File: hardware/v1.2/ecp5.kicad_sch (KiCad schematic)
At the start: 8 parts, among them U1 ECP5U_25F_CABGA256

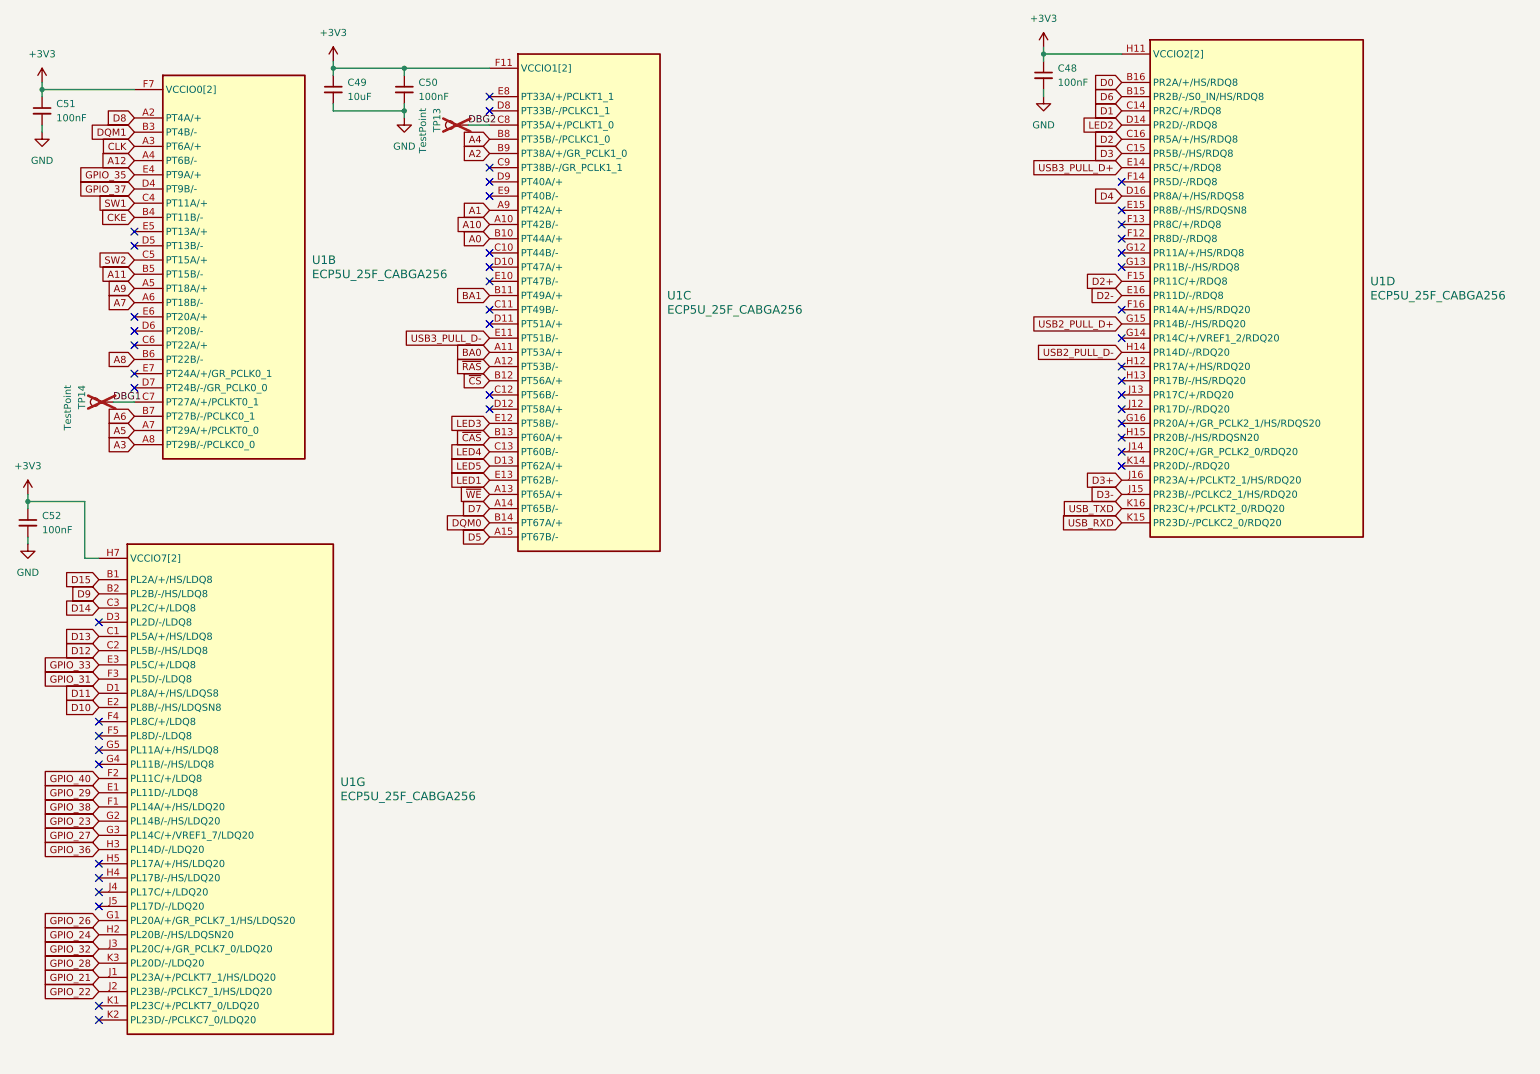
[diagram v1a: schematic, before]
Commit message: Custom ECP5-CABGA256 symbol
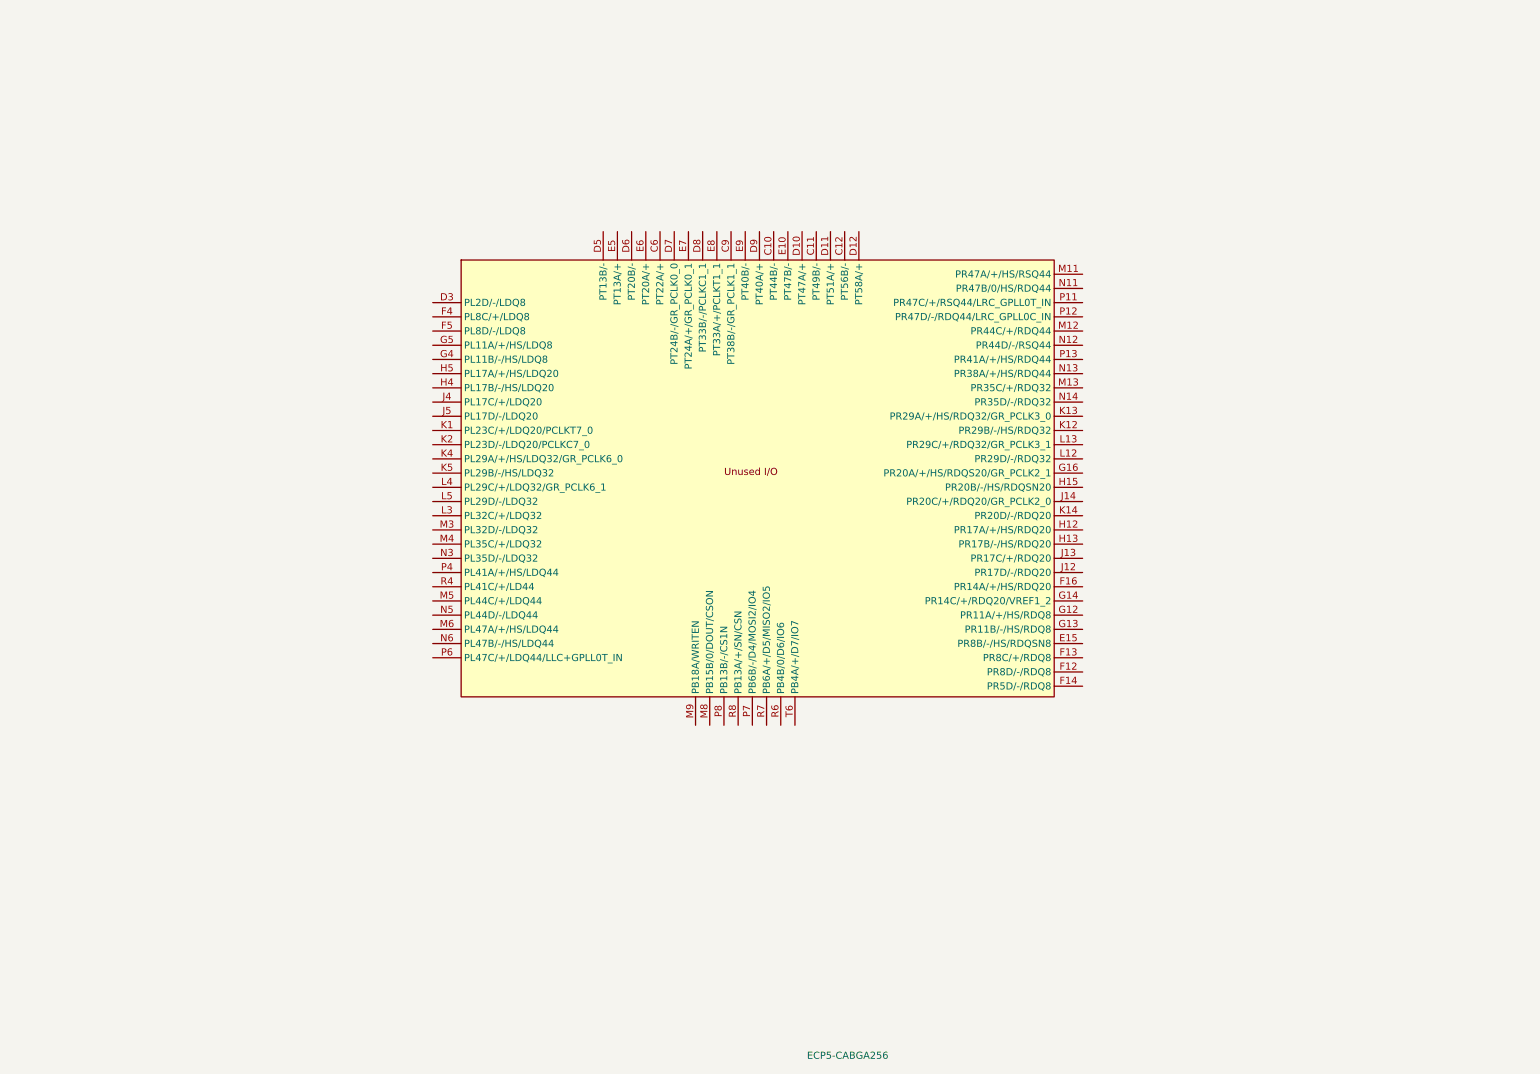
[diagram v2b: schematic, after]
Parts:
- removed C48, C50, C51, C52: 100nF, Capacitor_SMD:C_0402_1005Metric, symbol Device:C_Small
- removed C49: 10uF, Capacitor_SMD:C_0603_1608Metric, symbol Device:C_Small
- removed TP13, TP14: TestPoint, TestPoint:TestPoint_Pad_D1.0mm, symbol Connector:TestPoint
- removed U1: ECP5U_25F_CABGA256, Package_BGA:BGA-256_14.0x14.0mm_Layout16x16_P0.8mm_Ball0.45mm_Pad0.32mm_NSMD, symbol josh:ECP5U_12_CABGA256
- added U1: ECP5-CABGA256, Package_BGA:BGA-256_14.0x14.0mm_Layout16x16_P0.8mm_Ball0.45mm_Pad0.32mm_NSMD, symbol icepi-lib:LFE5U-25F-6BG256x
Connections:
- no-connect marks 46 -> 0

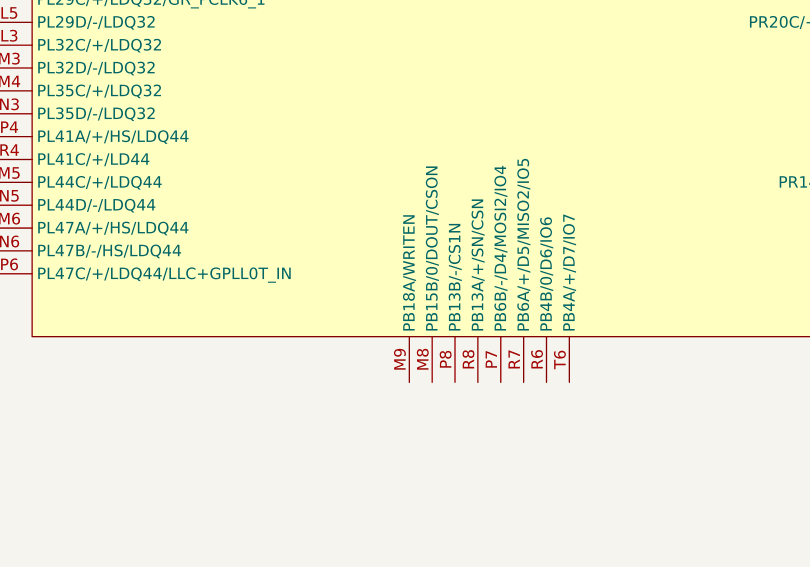
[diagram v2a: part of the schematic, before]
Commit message: UART to PS2 converter
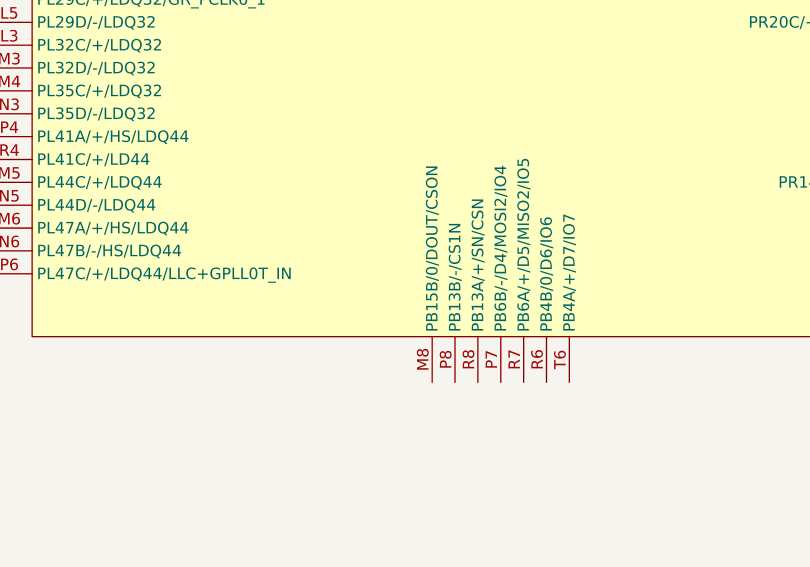
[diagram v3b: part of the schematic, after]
